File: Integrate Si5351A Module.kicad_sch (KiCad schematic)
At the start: 7 parts, among them J1 DC-005-5A-2.0, J2 TYPE-C-31-M-12, U1 USBLC6-2SC6

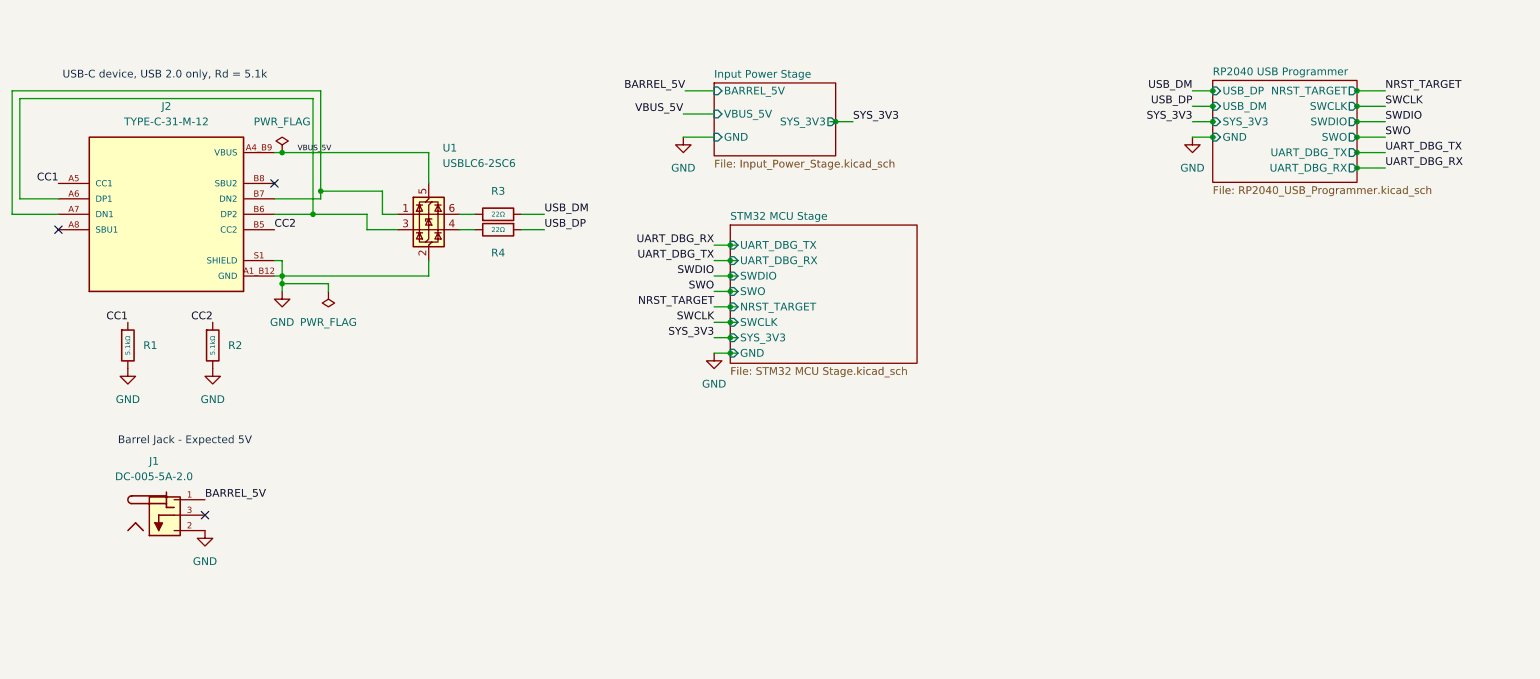
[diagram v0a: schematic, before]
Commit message: RF Module Stage Schematic Complete
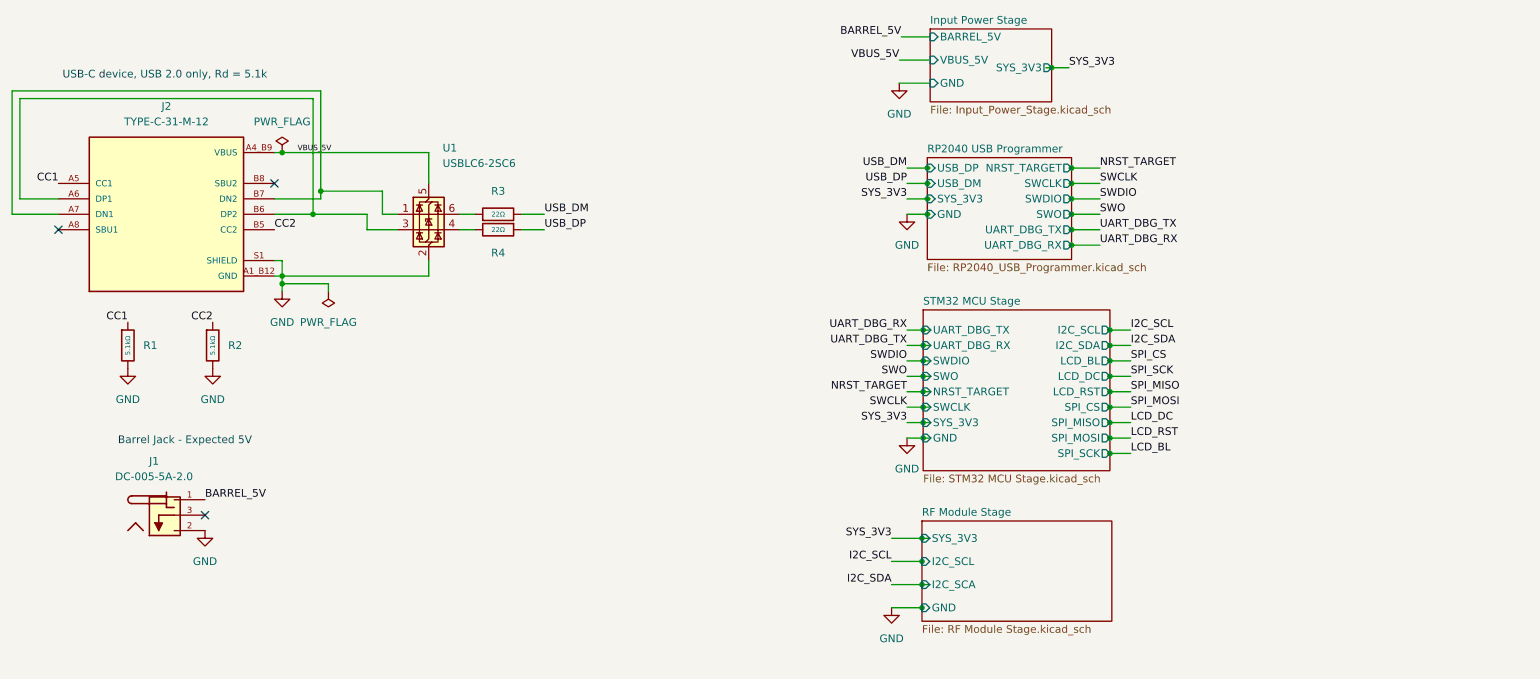
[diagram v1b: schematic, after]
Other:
- added sheet RF Module Stage (RF Module Stage.kicad_sch)
- sheet STM32 MCU Stage ports: added I2C_SCL, I2C_SDA, LCD_BL, LCD_DC, LCD_RST, SPI_CS, SPI_MISO, SPI_MOSI, SPI_SCK; removed none

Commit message: LCD Stage Finished
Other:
- added sheet LCD Module Stage (LCD Module Stage.kicad_sch)
- sheet STM32 MCU Stage ports: added none; removed SPI_MISO

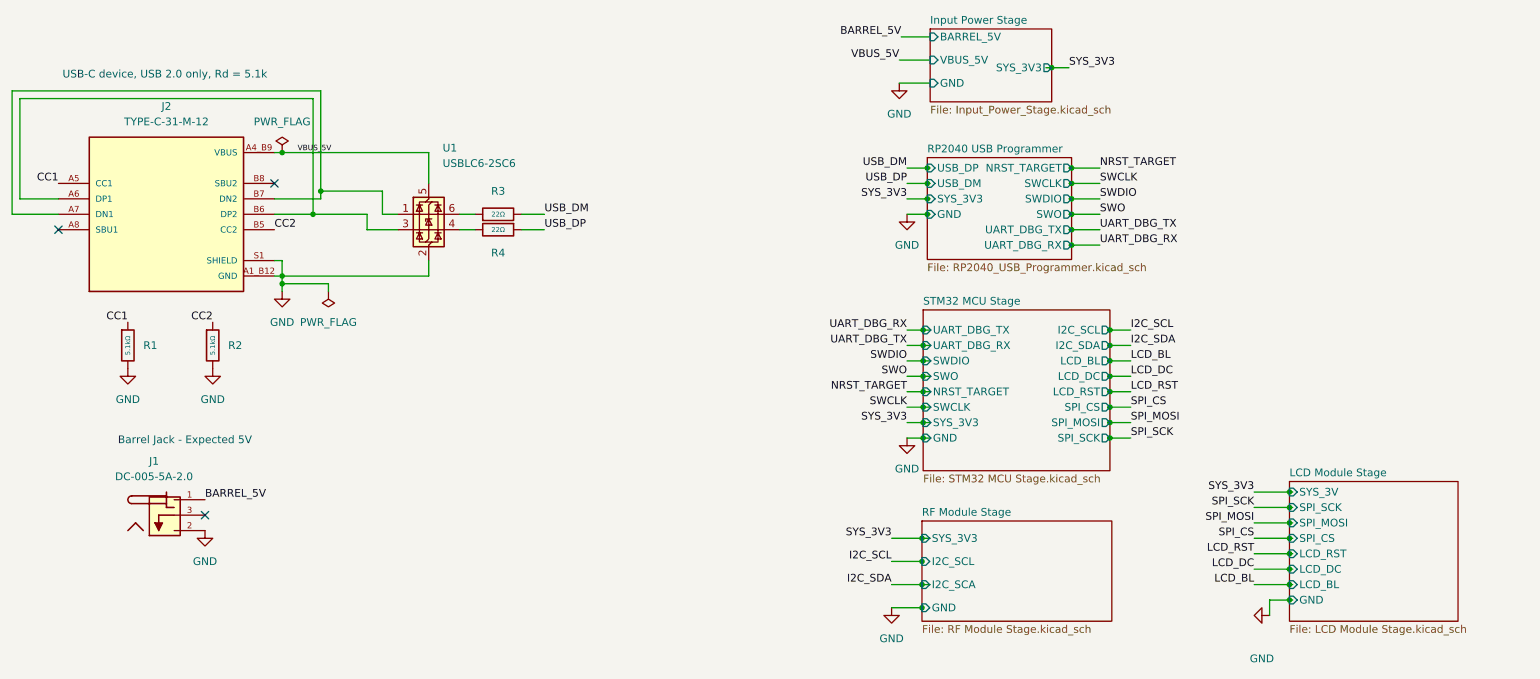
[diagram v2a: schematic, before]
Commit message: - Added Hysteresis resistor on TLV431BSN1T1G - Lowered TLV431BSN1T1G impedance values for resistors on the voltage divider
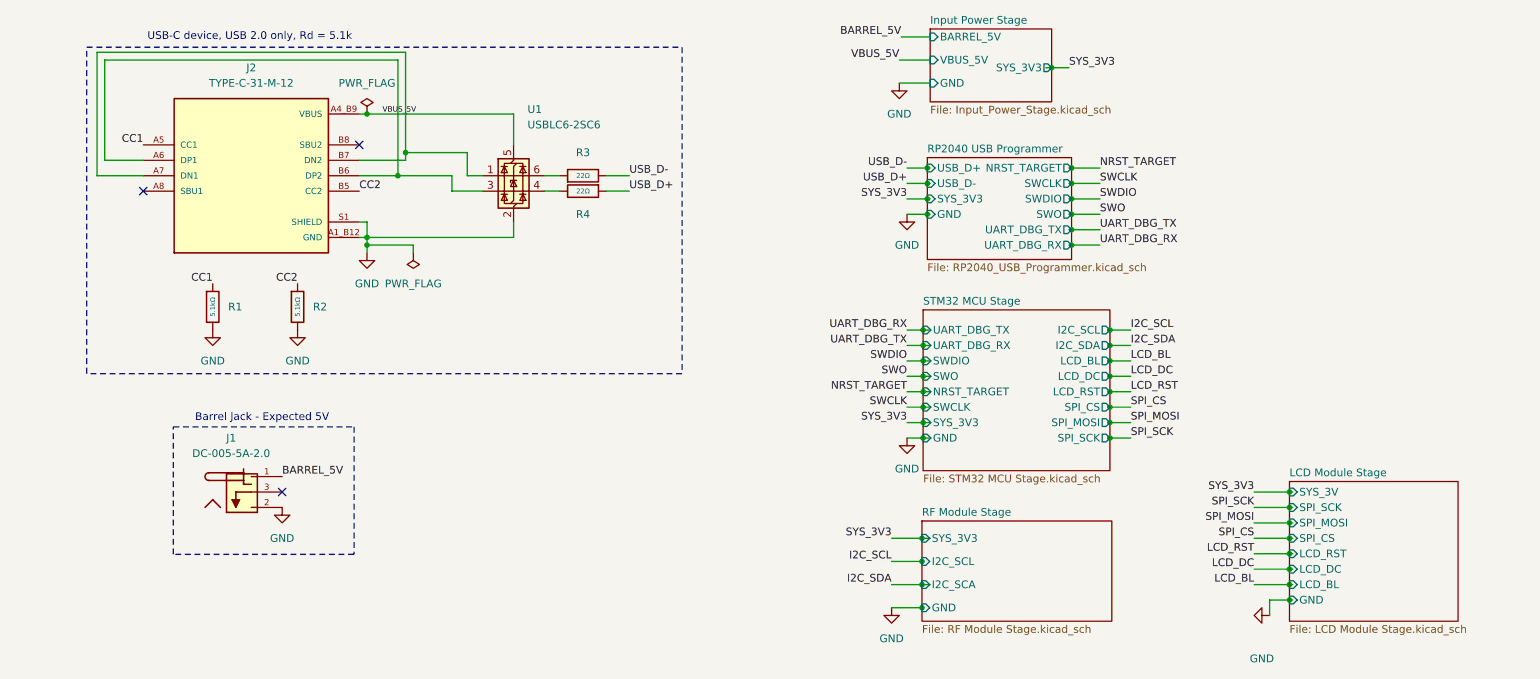
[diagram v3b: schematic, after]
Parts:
- J1: footprint DC-005-5A-2.0:XKB_DC-005-5A-2.0 -> 5V - DC Connector - DC-005-5A-2.0:XKB_DC-005-5A-2.0
- J2: footprint TYPE-C-31-M-12:HRO_TYPE-C-31-M-12 -> TYPE-C-31-M-12 -USB-C Input connector:HRO_TYPE-C-31-M-12
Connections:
- net USB_DM renamed USB_D-
- net USB_DP renamed USB_D+
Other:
- sheet RP2040 USB Programmer ports: added USB_D+, USB_D-; removed USB_DM, USB_DP
- company: Yaniv Lieberman -> (none)
- moved on the sheet: J1, J2, R1, R2, R3, R4, U1

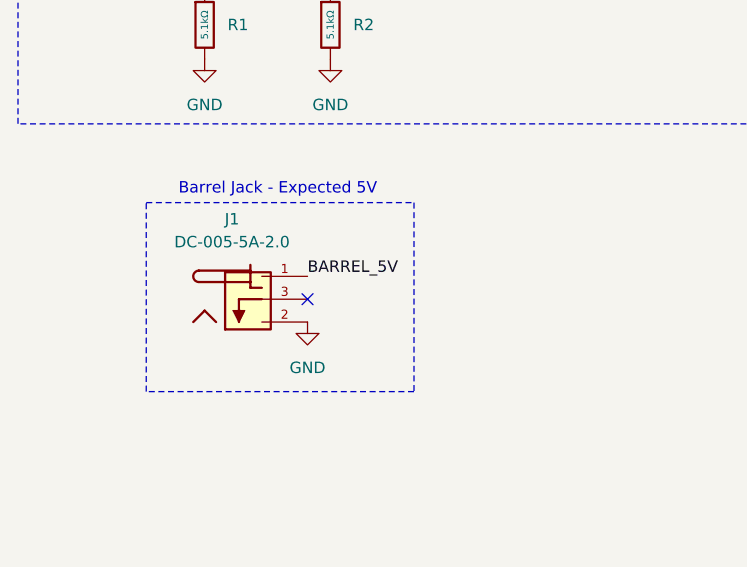
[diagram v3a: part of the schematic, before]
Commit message: - Added reverse polarity protection for barrel jack
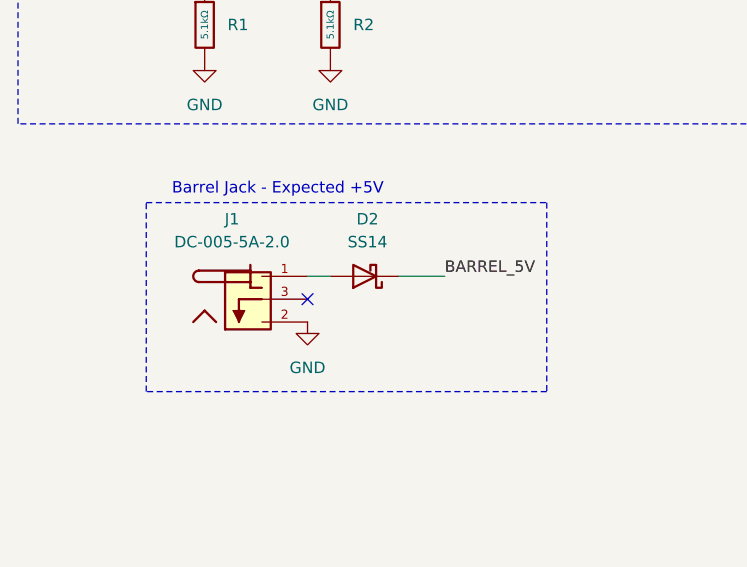
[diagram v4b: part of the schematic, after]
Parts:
- added D2: SS14, Diode_SMD:D_SMA, symbol Diode:SS14
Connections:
- net BARREL_5V: now also D2.1 (K); no longer J1.1
- new net: D2.2 (A), J1.1
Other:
- note added: "Barrel Jack - Expected +5V"
- note removed: "Barrel Jack - Expected 5V"
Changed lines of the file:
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@@
 	(rectangle
 		(start 40.5 83.25)
-		(end 70.25 104.25)
+		(end 85 104.25)
 		(stroke
 			(width 0)
@@
 		)
 	)
-	(text "Barrel Jack - Expected 5V"
+	(text "Barrel Jack - Expected +5V"
 		(exclude_from_sim no)
 		(at 55.118 81.788 0)
@@
 	(wire
 		(pts
+			(xy 68.58 91.44) (xy 73.66 91.44)
+		)
+		(stroke
+			(width 0)
+			(type default)
+		)
+	)
+	(wire
+		(pts
 			(xy 163.75 105.41) (xy 163.83 105.41)
 		)
@@
 	(wire
 		(pts
+			(xy 58.42 91.44) (xy 60.96 91.44)
+		)
+		(stroke
+			(width 0)
+			(type default)
+		)
+	)
+	(wire
+		(pts
 			(xy 29.21 22.86) (xy 77.47 22.86)
 		)
@@
 		)
 	)
-	(label "UART_DBG_TX"
-		(at 193.04 50.8 0)
+	(label "BARREL_5V"
+		(at 73.66 91.44 0)
 		(effects
 			(font
@@
 		)
 	)
-	(label "SPI_SCK"
-		(at 218.44 96.52 180)
+	(label "UART_DBG_TX"
+		(at 193.04 50.8 0)
 		(effects
 			(font
 				(size 1.27 1.27)
 			)
-			(justify right bottom)
+			(justify left bottom)
 		)
 	)
-	(label "BARREL_5V"
-		(at 58.42 91.44 0)
+	(label "SPI_SCK"
+		(at 218.44 96.52 180)
 		(effects
 			(font
 				(size 1.27 1.27)
 			)
-			(justify left bottom)
+			(justify right bottom)
 		)
 	)
@@
 					(unit 1)
 				)
+			)
+		)
+	)
+	(symbol
+		(lib_id "Diode:SS14")
+		(at 64.77 91.44 180)
+		(unit 1)
+		(exclude_from_sim no)
+		(in_bom yes)
+		(on_board yes)
+		(dnp no)
+		(fields_autoplaced yes)
+		(property "Reference" "D2"
+			(at 65.0875 85.09 0)
+			(effects
+				(font
+					(size 1.27 1.27)
+				)
+			)
+		)
+		(property "Value" "SS14"
+			(at 65.0875 87.63 0)
+			(effects
+				(font
+					(size 1.27 1.27)
+				)
+			)
+		)
+		(property "Footprint" "Diode_SMD:D_SMA"
+			(at 64.77 86.995 0)
+			(effects
+				(font
+					(size 1.27 1.27)
+				)
+				(hide yes)
+			)
+		)
+		(property "Datasheet" "https://www.vishay.com/docs/88746/ss12.pdf"
+			(at 64.77 91.44 0)
+			(effects
+				(font
+					(size 1.27 1.27)
+				)
+				(hide yes)
+			)
+		)
+		(property "Description" "40V 1A Schottky Diode, SMA"
+			(at 64.77 91.44 0)
+			(effects
+				(font
+					(size 1.27 1.27)
+				)
+				(hide yes)
+			)
+		)
+		(pin "2"
+		)
+		(pin "1"
+		)
+		(instances
+			(project ""
+				(path "/5effc93d-4636-458a-a65b-e63d3c617be7"
+					(reference "D2")
+					(unit 1)
+				)

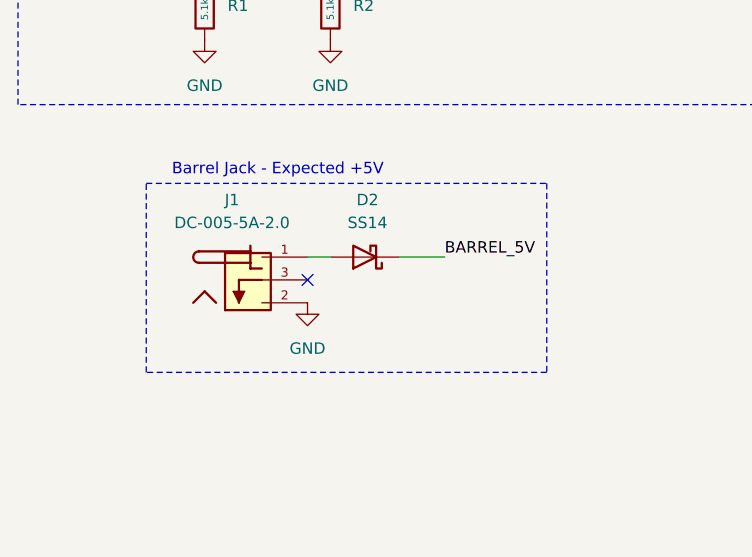
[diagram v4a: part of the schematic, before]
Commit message: - Added TVS ESD Protection diode on J1
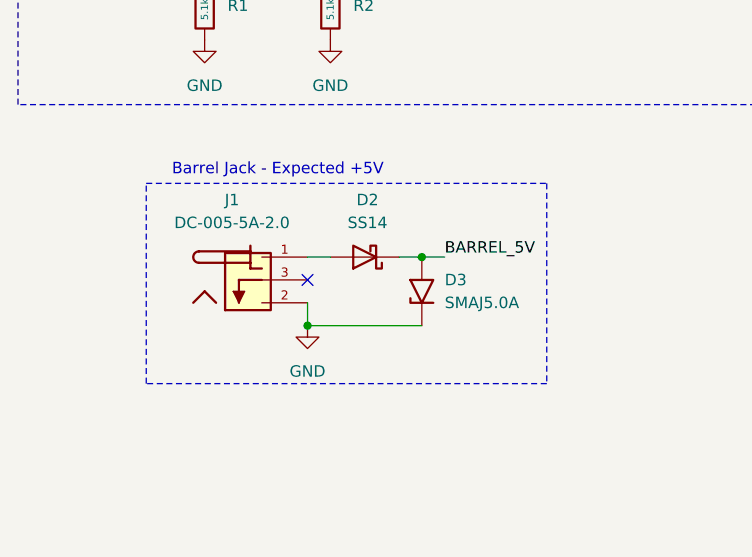
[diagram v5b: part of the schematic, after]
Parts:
- added D3: SMAJ5.0A, Diode_SMD:D_SMA, symbol Diode:SMAJ5.0A
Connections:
- net BARREL_5V: now also D3.2 (A2)
- net GND: now also D3.1 (A1)
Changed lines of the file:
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@@
 	(rectangle
 		(start 40.5 83.25)
-		(end 85 104.25)
+		(end 85 105.5)
 		(stroke
 			(width 0)
@@
 	)
 	(junction
+		(at 58.42 99.06)
+		(diameter 0)
+		(color 0 0 0 0)
+	)
+	(junction
 		(at 224.25 99.06)
 		(diameter 0)
@@
 	)
 	(junction
+		(at 71.12 91.44)
+		(diameter 0)
+		(color 0 0 0 0)
+	)
+	(junction
 		(at 78.74 38.1)
 		(diameter 0)
@@
 	(wire
 		(pts
+			(xy 58.42 99.06) (xy 58.42 96.52)
+		)
+		(stroke
+			(width 0)
+			(type default)
+		)
+	)
+	(wire
+		(pts
 			(xy 187.96 40.64) (xy 188.38 40.64)
 		)
@@
 	(wire
 		(pts
-			(xy 68.58 91.44) (xy 73.66 91.44)
+			(xy 68.58 91.44) (xy 71.12 91.44)
 		)
 		(stroke
@@
 	(wire
 		(pts
+			(xy 58.42 99.06) (xy 71.12 99.06)
+		)
+		(stroke
+			(width 0)
+			(type default)
+		)
+	)
+	(wire
+		(pts
 			(xy 71.12 52.07) (xy 72.39 52.07)
 		)
@@
 	(wire
 		(pts
+			(xy 71.12 91.44) (xy 73.66 91.44)
+		)
+		(stroke
+			(width 0)
+			(type default)
+		)
+	)
+	(wire
+		(pts
 			(xy 161.29 74.93) (xy 163.94 74.93)
 		)
@@
 	(symbol
 		(lib_id "power:GND")
-		(at 58.42 96.52 0)
+		(at 58.42 99.06 0)
 		(unit 1)
 		(exclude_from_sim no)
@@
 		(fields_autoplaced yes)
 		(property "Reference" "#PWR02"
-			(at 58.42 102.87 0)
+			(at 58.42 105.41 0)
 			(effects
 				(font
@@
 		)
 		(property "Value" "GND"
-			(at 58.42 101.6 0)
+			(at 58.42 104.14 0)
 			(effects
 				(font
@@
 		)
 		(property "Footprint" ""
-			(at 58.42 96.52 0)
+			(at 58.42 99.06 0)
 			(effects
 				(font
@@
 		)
 		(property "Datasheet" ""
-			(at 58.42 96.52 0)
+			(at 58.42 99.06 0)
 			(effects
 				(font
@@
 		)
 		(property "Description" "Power symbol creates a global label with name \"GND\" , ground"
-			(at 58.42 96.52 0)
+			(at 58.42 99.06 0)
 			(effects
 				(font
@@
 					(unit 1)
 				)
+			)
+		)
+	)
+	(symbol
+		(lib_id "Diode:SMAJ5.0A")
+		(at 71.12 95.25 90)
+		(unit 1)
+		(exclude_from_sim no)
+		(in_bom yes)
+		(on_board yes)
+		(dnp no)
+		(fields_autoplaced yes)
+		(property "Reference" "D3"
+			(at 73.66 93.9799 90)
+			(effects
+				(font
+					(size 1.27 1.27)
+				)
+				(justify right)
+			)
+		)
+		(property "Value" "SMAJ5.0A"
+			(at 73.66 96.5199 90)
+			(effects
+				(font
+					(size 1.27 1.27)
+				)
+				(justify right)
+			)
+		)
+		(property "Footprint" "Diode_SMD:D_SMA"
+			(at 76.2 95.25 0)
+			(effects
+				(font
+					(size 1.27 1.27)
+				)
+				(hide yes)
+			)
+		)
+		(property "Datasheet" "https://www.littelfuse.com/media?resourcetype=datasheets&itemid=75e32973-b177-4ee3-a0ff-cedaf1abdb93&filename=smaj-datasheet"
+			(at 71.12 96.52 0)
+			(effects
+				(font
+					(size 1.27 1.27)
+				)
+				(hide yes)
+			)
+		)
+		(property "Description" "400W unidirectional Transient Voltage Suppressor, 5.0Vr, SMA(DO-214AC)"
+			(at 71.12 95.25 0)
+			(effects
+				(font
+					(size 1.27 1.27)
+				)
+				(hide yes)
+			)
+		)
+		(pin "1"
+		)
+		(pin "2"
+		)
+		(instances
+			(project ""
+				(path "/5effc93d-4636-458a-a65b-e63d3c617be7"
+					(reference "D3")
+					(unit 1)
+				)

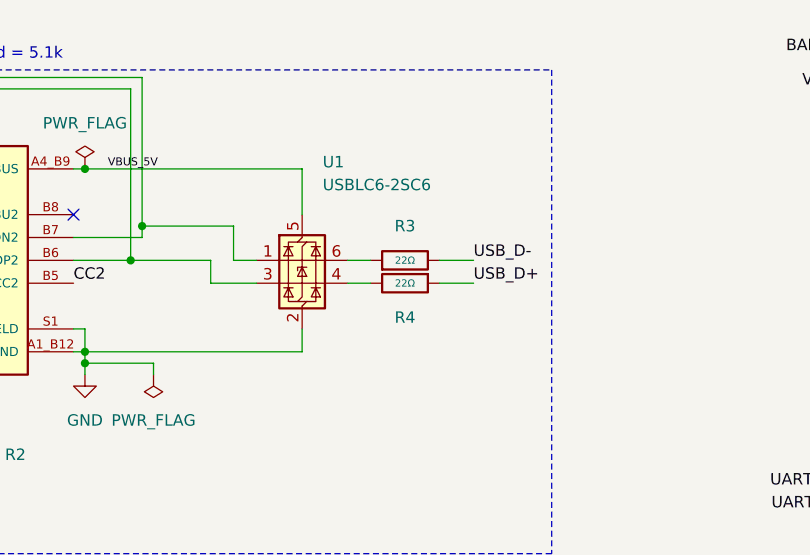
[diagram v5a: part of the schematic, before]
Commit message: Changed values of R3 and R4 to comply with USB RP guidelines
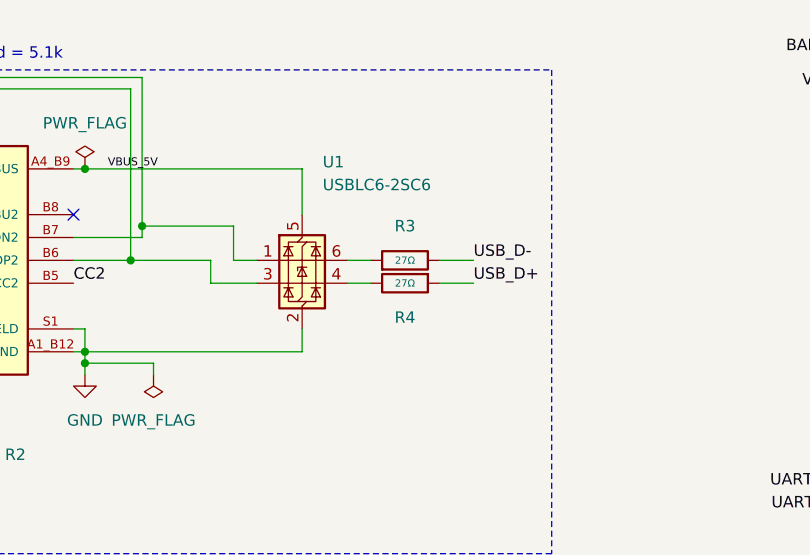
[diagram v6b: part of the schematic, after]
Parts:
- R3, R4: value 22Ω -> 27Ω
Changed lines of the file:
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@@
 			)
 		)
-		(property "Value" "22Ω"
+		(property "Value" "27Ω"
 			(at 107.95 44.45 90)
 			(do_not_autoplace yes)
@@
 			)
 		)
-		(property "Value" "22Ω"
+		(property "Value" "27Ω"
 			(at 107.95 41.91 90)
 			(do_not_autoplace yes)
